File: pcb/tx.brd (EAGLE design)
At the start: 28 x 35 mm, 52 parts, among them U3 MCP73831T-2ACI/OT, Y1 CRYSTAL-26MHZSMD-3.2X2.5

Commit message: txrx rev2 finished
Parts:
- added R13: 22K, joyAnalog:0805
- moved SJ2 3.86 mm to (23.9, 5.59), turned to 90 degrees
- moved LED2 0.55 mm to (5.84, 23.3)
- moved U$5 0.50 mm to (2.50, 27.0)
- moved U$6 0.50 mm to (25.5, 27.0)
- moved U$10 0.23 mm to (1.68, 21.6)
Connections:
- new net N$36: SJ2.2, U$2.6
- net +3V3: now also U$10.P$1, U$10.P$4
- net GND: now also R13.2; no longer U$10.P$1, U$10.P$4
- net N$30: now also R13.1
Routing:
- net GND: track 39.6 -> 30.6 mm
- net N$36: track 0.00 -> 7.97 mm, vias 0 -> 1
- net +3V3: track 43.8 -> 48.0 mm, vias 7 -> 9
- net N$30: track 26.7 -> 28.8 mm
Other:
- board text added: "ADDR"
- board text added: "REV2 FEB19"
- board text added: "dekuNukem 2018"
- board text removed: "TEST"
- board text removed: "dayTripper TX dekuNukem 2018"

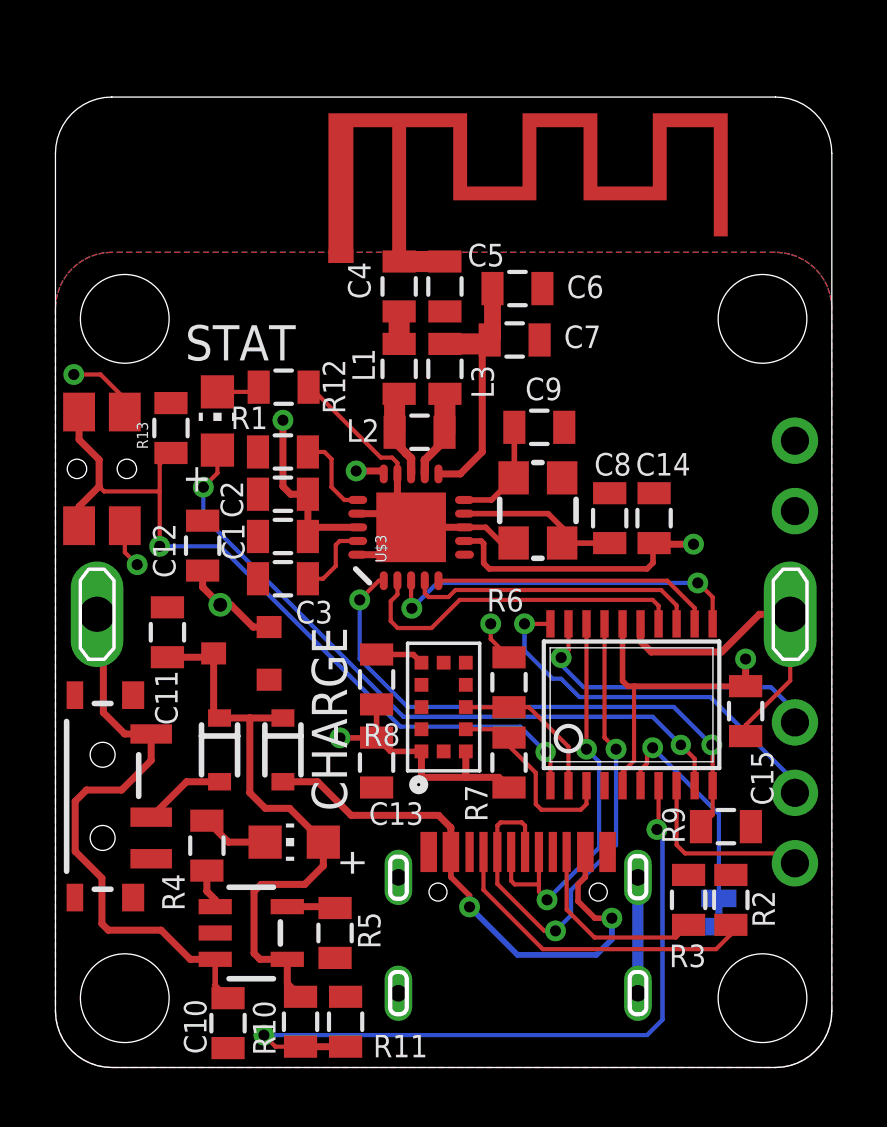
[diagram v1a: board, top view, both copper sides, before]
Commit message: switched to chip antenna
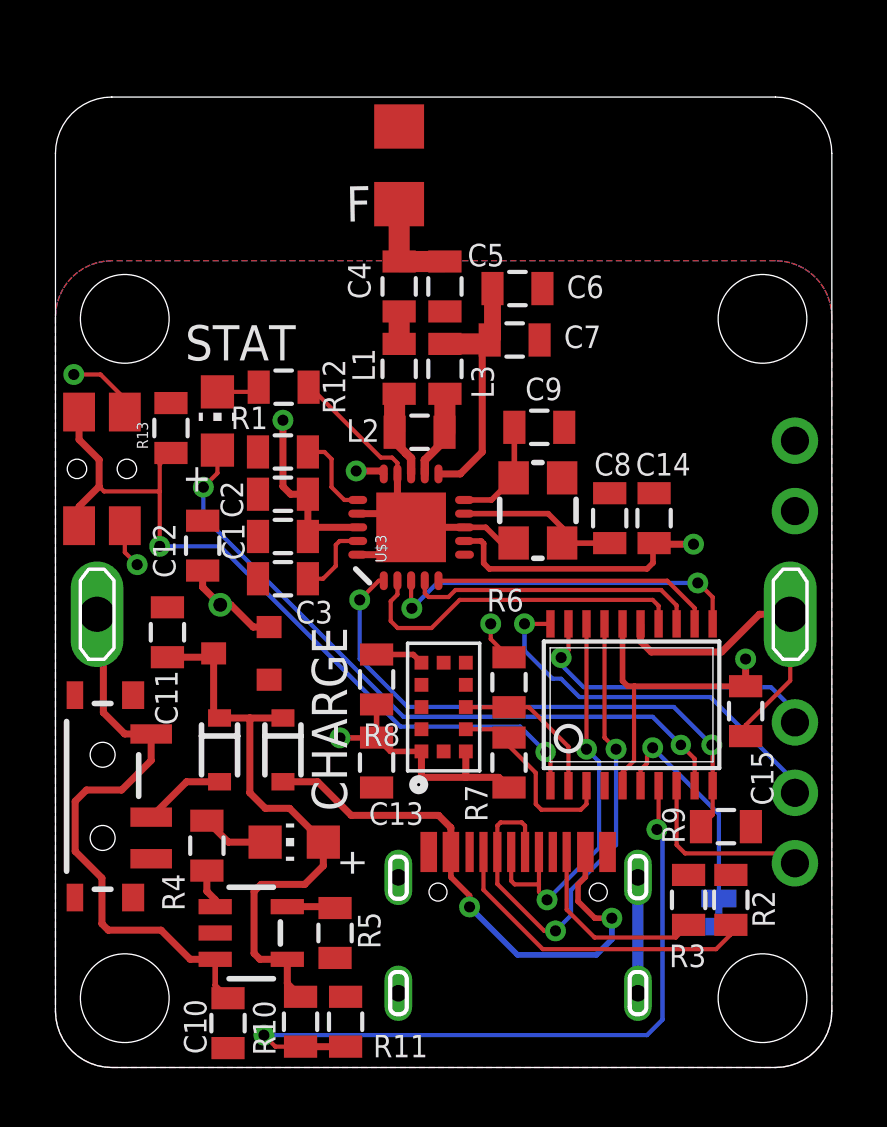
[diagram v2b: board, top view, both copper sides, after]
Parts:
- removed E1: ANT, SparkFun-RF:TRACE_ANTENNA_2.4GHZ_15.2MM
- added U$1: 1206ANT_DEV, 3pos_slide_switch:C1206
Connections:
- net GND: no longer E1.GND
- net N$5: now also U$1.1; no longer E1.ANT
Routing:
- net N$5: track 1.85 -> 3.72 mm
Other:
- board text added: "DFU"
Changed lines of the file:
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@@
 <grid distance="2" unitdist="mil" unit="mil" style="lines" multiple="1" display="no" altdistance="5" altunitdist="mil" altunit="mil"/>
 <layers>
-<layer number="1" name="Top" color="4" fill="1" visible="no" active="yes"/>
+<layer number="1" name="Top" color="4" fill="1" visible="yes" active="yes"/>
 <layer number="2" name="Route2" color="16" fill="1" visible="no" active="no"/>
 <layer number="3" name="Route3" color="17" fill="1" visible="no" active="no"/>
@@
 <layer number="19" name="Unrouted" color="6" fill="1" visible="yes" active="yes"/>
 <layer number="20" name="Dimension" color="24" fill="1" visible="yes" active="yes"/>
-<layer number="21" name="tPlace" color="7" fill="1" visible="no" active="yes"/>
+<layer number="21" name="tPlace" color="7" fill="1" visible="yes" active="yes"/>
 <layer number="22" name="bPlace" color="7" fill="1" visible="yes" active="yes"/>
-<layer number="23" name="tOrigins" color="15" fill="1" visible="no" active="yes"/>
+<layer number="23" name="tOrigins" color="15" fill="1" visible="yes" active="yes"/>
 <layer number="24" name="bOrigins" color="15" fill="1" visible="yes" active="yes"/>
-<layer number="25" name="tNames" color="7" fill="1" visible="no" active="yes"/>
+<layer number="25" name="tNames" color="7" fill="1" visible="yes" active="yes"/>
 <layer number="26" name="bNames" color="7" fill="1" visible="yes" active="yes"/>
 <layer number="27" name="tValues" color="7" fill="1" visible="no" active="yes"/>
@@
 <layer number="37" name="tTest" color="7" fill="1" visible="no" active="yes"/>
 <layer number="38" name="bTest" color="7" fill="1" visible="no" active="yes"/>
-<layer number="39" name="tKeepout" color="4" fill="11" visible="no" active="yes"/>
+<layer number="39" name="tKeepout" color="4" fill="11" visible="yes" active="yes"/>
 <layer number="40" name="bKeepout" color="1" fill="11" visible="yes" active="yes"/>
-<layer number="41" name="tRestrict" color="4" fill="10" visible="no" active="yes"/>
+<layer number="41" name="tRestrict" color="4" fill="10" visible="yes" active="yes"/>
 <layer number="42" name="bRestrict" color="1" fill="10" visible="yes" active="yes"/>
 <layer number="43" name="vRestrict" color="2" fill="10" visible="no" active="yes"/>
@@
 <layer number="49" name="Reference" color="7" fill="1" visible="no" active="yes"/>
 <layer number="50" name="dxf" color="7" fill="1" visible="no" active="no"/>
-<layer number="51" name="tDocu" color="7" fill="1" visible="no" active="yes"/>
+<layer number="51" name="tDocu" color="7" fill="1" visible="yes" active="yes"/>
 <layer number="52" name="bDocu" color="7" fill="1" visible="yes" active="yes"/>
 <layer number="53" name="tGND_GNDA" color="7" fill="1" visible="no" active="no"/>
@@
 <wire x1="2.032" y1="0" x2="25.968" y2="0" width="0" layer="20"/>
 <wire x1="25.968" y1="0" x2="28" y2="2.032" width="0" layer="20" curve="90"/>
-<polygon width="0.254" layer="41">
-<vertex x="11.8364" y="28.7782"/>
-<vertex x="11.8364" y="29.8958"/>
-<vertex x="12.8524" y="29.8958"/>
-<vertex x="12.8524" y="28.7782"/>
-</polygon>
 <text x="25.273" y="21.971" size="1.27" layer="26" rot="MR0">GND</text>
 <text x="25.273" y="19.431" size="1.27" layer="26" rot="MR0">3V</text>
@@
 <text x="8.6614" y="26.7716" size="1.27" layer="25" rot="R180">STAT</text>
 <text x="23.0886" y="6.3754" size="0.8128" layer="26" rot="MR270">ADDR</text>
+<text x="1.9304" y="22.7584" size="1.27" layer="26" rot="MR270">DFU</text>
 </plain>
 <attributes>
@@
 </element>
 <element name="SJ2" library="SparkFun-Jumpers" package="SMT-JUMPER_2_NC_TRACE_NO-SILK" value="JUMPER-SMT_2_NC_TRACE_NO-SILK" x="23.9268" y="5.588" smashed="yes" rot="MR90"/>
-<element name="E1" library="SparkFun-RF" package="TRACE_ANTENNA_2.4GHZ_15.2MM" value="ANT" x="12.3952" y="29.5148" smashed="yes">
-<attribute name="VALUE" x="12.3952" y="30.5308" size="0.6096" layer="27" font="vector" ratio="20" align="top-center"/>
-</element>
 <element name="U$4" library="my_usbc_16p" package="USBC_16P_FOOT" value="USBC_16P" x="13.462" y="7.7724"/>
 <element name="R13" library="joyAnalog" package="0805" value="22K" x="4.1656" y="23.0632" rot="R90"/>
+<element name="U$1" library="3pos_slide_switch" package="C1206" value="1206ANT_DEV" x="12.3952" y="32.5374" rot="R90"/>
 </elements>
 <signals>
@@
 <contactref element="BT1" pad="2"/>
 <polygon width="0.1524" layer="1" isolate="0.254">
-<vertex x="28" y="2.032"/>
-<vertex x="28" y="27.3696" curve="90"/>
-<vertex x="25.968" y="29.4016"/>
-<vertex x="2.032" y="29.4016" curve="90"/>
-<vertex x="0" y="27.3696"/>
+<vertex x="25.968" y="29.0968"/>
+<vertex x="2.032" y="29.0968" curve="90"/>
+<vertex x="0" y="27.0648"/>
 <vertex x="0" y="2.032" curve="90"/>
 <vertex x="2.032" y="0"/>
 <vertex x="25.968" y="0" curve="90"/>
+<vertex x="28" y="2.032"/>
+<vertex x="28" y="27.0648" curve="90"/>
 </polygon>
 <contactref element="C10" pad="2"/>
@@
 <wire x1="11.7348" y1="21.9964" x2="9.1948" y2="24.5364" width="0.1524" layer="1"/>
 <wire x1="9.1948" y1="24.5364" x2="9.1296" y2="24.5364" width="0.1524" layer="1"/>
-<contactref element="E1" pad="GND"/>
 <contactref element="U$4" pad="B11A12"/>
 <contactref element="U$4" pad="P$13"/>
@@
 <contactref element="C12" pad="1"/>
 <polygon width="0.1524" layer="16" isolate="0.254">
-<vertex x="28" y="2.032"/>
-<vertex x="28" y="27.3696" curve="90"/>
-<vertex x="25.968" y="29.4016"/>
-<vertex x="2.032" y="29.4016" curve="90"/>
-<vertex x="0" y="27.3696"/>
+<vertex x="25.968" y="29.0968"/>
+<vertex x="2.032" y="29.0968" curve="90"/>
+<vertex x="0" y="27.0648"/>
 <vertex x="0" y="2.032" curve="90"/>
 <vertex x="2.032" y="0"/>
 <vertex x="25.968" y="0" curve="90"/>
+<vertex x="28" y="2.032"/>
+<vertex x="28" y="27.0648" curve="90"/>
 </polygon>
 <via x="5.9436" y="16.6878" extent="1-16" drill="0.5"/>
@@
 <contactref element="C4" pad="2"/>
 <contactref element="C5" pad="1"/>
-<contactref element="E1" pad="ANT"/>
 <wire x1="14.0462" y1="29.0686" x2="12.3952" y2="29.0686" width="0.762" layer="1"/>
-<wire x1="12.3952" y1="29.0686" x2="12.3952" y2="29.2648" width="0.508" layer="1"/>
+<contactref element="U$1" pad="1"/>
+<wire x1="12.3952" y1="29.0686" x2="12.3952" y2="31.1374" width="0.762" layer="1"/>
 </signal>
 <signal name="N$6">

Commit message: GND plane, trace antenna, clean up
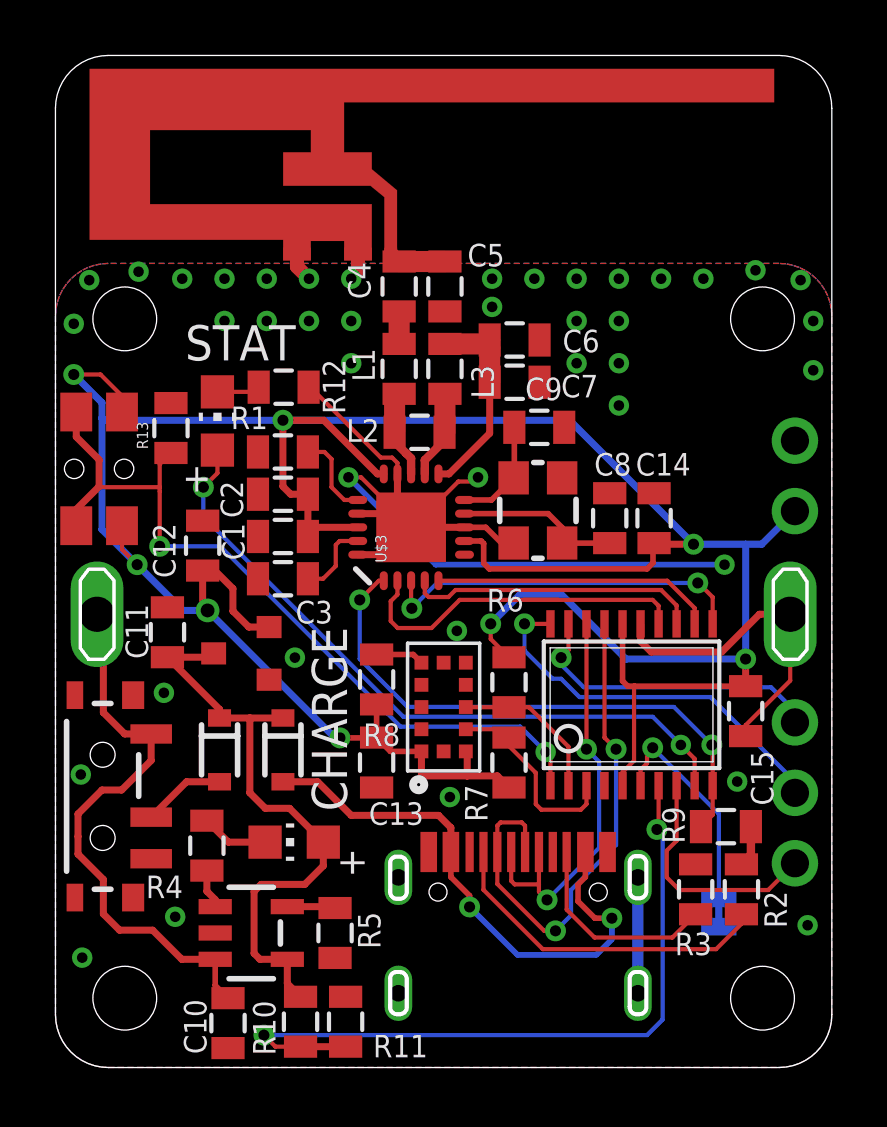
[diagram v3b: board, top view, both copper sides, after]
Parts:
- removed U$5, U$6, U$7, U$8: M3_MOUNTING_HOLE, L1:M3_MOUNTING_HOLE_PACK
- added E1: ANTENNA, esp32-thing-temp:TRACE_ANTENNA_2.4GHZ_25.7MM_TUNED
- added U$12, U$13, U$14: M2_SCREW_DEV, 3pos_slide_switch:M2_SCREW_FOOT
- U$1: value 1206ANT_DEV -> M2_SCREW_DEV; device 3pos_slide_switch:C1206 -> 3pos_slide_switch:M2_SCREW_FOOT
- moved U$1 31.6 mm to (2.50, 2.50), turned to 0 degrees
- moved C6 1.86 mm to (16.6, 26.2)
- moved C7 1.52 mm to (16.6, 24.7)
- moved R2 0.54 mm to (24.7, 6.43)
- moved R3 0.46 mm to (23.1, 6.43)
- moved U$10 0.10 mm to (1.57, 21.6)
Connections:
- net +3V3: no longer SJ2.1
- net GND: now also E1.GND, E1.GND2, SJ2.1
- net N$5: now also E1.ANT; no longer U$1.1
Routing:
- net +3V3: track 48.0 -> 112.8 mm, vias 9 -> 8
- net GND: track 30.6 -> 54.3 mm, vias 0 -> 41
- net N$8: track 9.63 -> 7.41 mm
- net N$33: track 6.68 -> 8.66 mm
- net N$5: track 3.72 -> 2.07 mm
- net N$27: track 21.3 -> 22.1 mm
- net N$25: track 21.0 -> 20.4 mm
- net N$11: track 11.7 -> 12.3 mm
- added copper zone on layer 16, net GND
- removed copper zone on layer 16, net +3V3
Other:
- board size 28 x 35 mm -> 28 x 36.5 mm
- board text added: "CH"
- board text added: "REV3 FEB19"
- board text removed: "ADDR"
- board text removed: "REV2 FEB19"

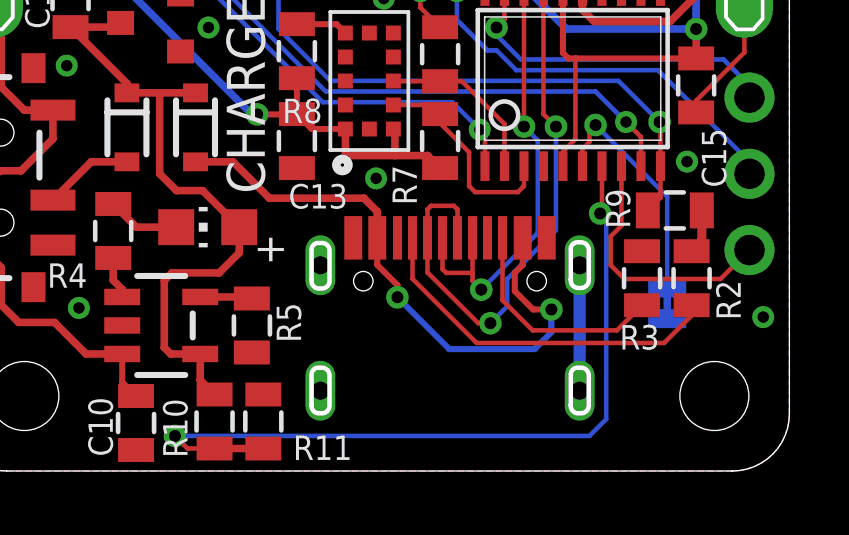
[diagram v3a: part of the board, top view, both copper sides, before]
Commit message: changed copyright date
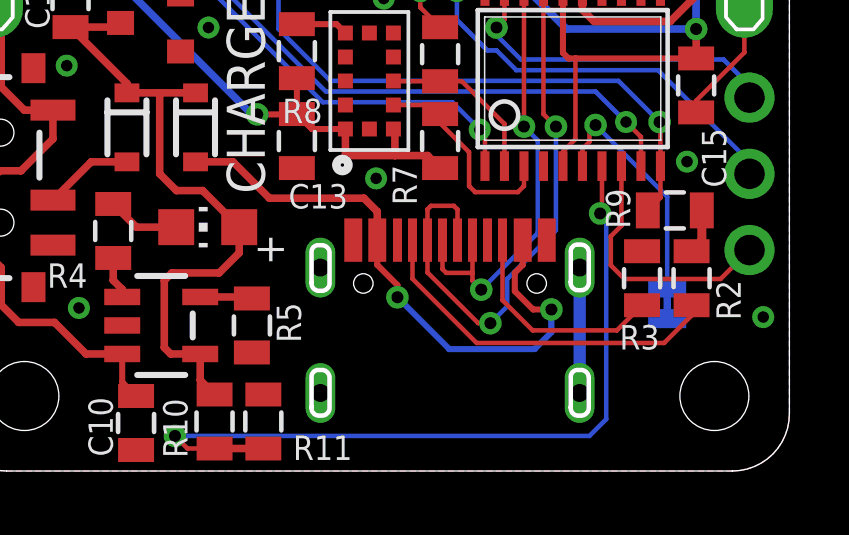
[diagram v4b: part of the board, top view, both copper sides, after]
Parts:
- moved U$4 0.08 mm to (13.5, 7.70)
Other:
- board text added: "dekuNukem 2019"
- board text removed: "dekuNukem 2018"
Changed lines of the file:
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@@
 <setting verticaltext="up"/>
 </settings>
-<grid distance="2" unitdist="mil" unit="mil" style="lines" multiple="1" display="no" altdistance="1" altunitdist="mil" altunit="mil"/>
+<grid distance="1" unitdist="mil" unit="mil" style="lines" multiple="1" display="no" altdistance="1" altunitdist="mil" altunit="mil"/>
 <layers>
 <layer number="1" name="Top" color="4" fill="1" visible="yes" active="yes"/>
@@
 <text x="25.273" y="9.271" size="1.27" layer="26" rot="MR0">CLK</text>
 <text x="25.273" y="6.731" size="1.27" layer="26" rot="MR0">TX</text>
-<text x="14" y="31.017" size="1.016" layer="26" font="vector" rot="MR0" align="center">dekuNukem 2018</text>
+<text x="14" y="31.017" size="1.016" layer="26" font="vector" rot="MR0" align="center">dekuNukem 2019</text>
 <text x="14" y="33.205" size="1.27" layer="26" rot="MR0" align="center">git.io/daytripper</text>
 <text x="16.8402" y="2.032" size="1.27" layer="26" rot="MR0" align="center">REV3
@@
 </element>
 <element name="SJ2" library="SparkFun-Jumpers" package="SMT-JUMPER_2_NC_TRACE_NO-SILK" value="JUMPER-SMT_2_NC_TRACE_NO-SILK" x="23.9268" y="5.588" smashed="yes" rot="MR90"/>
-<element name="U$4" library="my_usbc_16p" package="USBC_16P_FOOT" value="USBC_16P" x="13.462" y="7.7724"/>
+<element name="U$4" library="my_usbc_16p" package="USBC_16P_FOOT" value="USBC_16P" x="13.462" y="7.6962"/>
 <element name="R13" library="joyAnalog" package="0805" value="22K" x="4.1656" y="23.0632" rot="R90"/>
 <element name="E1" library="esp32-thing-temp" package="TRACE_ANTENNA_2.4GHZ_25.7MM_TUNED" value="ANTENNA" x="12.0904" y="29.1084"/>
@@
 <wire x1="25.3884" y1="16.346" x2="26.5" y2="16.346" width="0.254" layer="1"/>
 <wire x1="24.0284" y1="14.986" x2="25.3884" y2="16.346" width="0.254" layer="1"/>
-<wire x1="21.007" y1="6.8574" x2="21.007" y2="2.6774" width="0.4064" layer="16"/>
+<wire x1="21.007" y1="6.7812" x2="21.007" y2="2.6012" width="0.4064" layer="16"/>
 <wire x1="26.5" y1="16.346" x2="26.5" y2="13.9524" width="0.1524" layer="1"/>
 <wire x1="24.892" y1="12.3444" x2="24.892" y2="11.9524" width="0.1524" layer="1"/>
@@
 <contactref element="U$4" pad="B5"/>
 <wire x1="22.2504" y1="4.688" x2="19.442" y2="4.688" width="0.1524" layer="1"/>
-<wire x1="18.437" y1="5.693" x2="18.437" y2="7.7724" width="0.1524" layer="1"/>
+<wire x1="18.437" y1="5.693" x2="18.437" y2="7.6962" width="0.1524" layer="1"/>
 <wire x1="19.442" y1="4.688" x2="18.437" y2="5.693" width="0.1524" layer="1"/>
 <wire x1="23.0886" y1="5.5262" x2="22.2504" y2="4.688" width="0.1524" layer="1"/>
@@
 <wire x1="24.7396" y1="5.1816" x2="23.8252" y2="4.2672" width="0.1524" layer="1"/>
 <wire x1="23.8252" y1="4.2672" x2="17.5768" y2="4.2672" width="0.1524" layer="1"/>
-<wire x1="15.437" y1="6.407" x2="15.437" y2="7.7724" width="0.1524" layer="1"/>
+<wire x1="15.437" y1="6.407" x2="15.437" y2="7.6962" width="0.1524" layer="1"/>
 <wire x1="17.5768" y1="4.2672" x2="15.437" y2="6.407" width="0.1524" layer="1"/>
 </signal>
@@
 <contactref element="U$4" pad="B4A9"/>
 <wire x1="10.668" y1="9.0932" x2="13.8176" y2="9.0932" width="0.254" layer="1"/>
-<wire x1="14.262" y1="8.6488" x2="14.262" y2="7.7724" width="0.254" layer="1"/>
+<wire x1="14.262" y1="8.6488" x2="14.262" y2="7.6962" width="0.254" layer="1"/>
 <wire x1="13.8176" y1="9.0932" x2="14.262" y2="8.6488" width="0.254" layer="1"/>
-<wire x1="19.112" y1="7.7724" x2="19.112" y2="6.8692" width="0.2032" layer="1"/>
+<wire x1="19.112" y1="7.6962" x2="19.112" y2="6.8692" width="0.2032" layer="1"/>
 <wire x1="19.112" y1="6.8692" x2="18.8468" y2="6.604" width="0.2032" layer="1"/>
 <wire x1="18.8468" y1="6.604" x2="18.8468" y2="5.9944" width="0.2032" layer="1"/>
@@
 <via x="14.9352" y="5.7912" extent="1-16" drill="0.4"/>
 <wire x1="14.9352" y1="5.7912" x2="14.9352" y2="6.1976" width="0.2032" layer="1"/>
-<wire x1="14.262" y1="6.8708" x2="14.262" y2="7.7724" width="0.2032" layer="1"/>
+<wire x1="14.262" y1="6.8708" x2="14.262" y2="7.6962" width="0.2032" layer="1"/>
 <wire x1="14.9352" y1="6.1976" x2="14.262" y2="6.8708" width="0.2032" layer="1"/>
 </signal>
@@
 <via x="19.1516" y="11.4808" extent="1-16" drill="0.4"/>
 <via x="17.7292" y="6.0452" extent="1-16" drill="0.4"/>
-<wire x1="17.437" y1="7.7724" x2="17.437" y2="6.604" width="0.1524" layer="1"/>
+<wire x1="17.437" y1="7.6962" x2="17.437" y2="6.604" width="0.1524" layer="1"/>
 <wire x1="17.437" y1="6.604" x2="17.437" y2="6.3374" width="0.1524" layer="1"/>
 <wire x1="17.437" y1="6.3374" x2="17.7292" y2="6.0452" width="0.1524" layer="1"/>
-<wire x1="16.437" y1="7.7724" x2="16.437" y2="6.7278" width="0.1524" layer="1"/>
+<wire x1="16.437" y1="7.6962" x2="16.437" y2="6.7278" width="0.1524" layer="1"/>
 <wire x1="16.437" y1="6.7278" x2="16.5608" y2="6.604" width="0.1524" layer="1"/>
 <wire x1="16.5608" y1="6.604" x2="17.437" y2="6.604" width="0.1524" layer="1"/>
@@
 <contactref element="U$4" pad="B7"/>
 <contactref element="U$2" pad="17"/>
-<wire x1="16.937" y1="7.7724" x2="16.937" y2="8.717" width="0.1524" layer="1"/>
+<wire x1="16.937" y1="7.6962" x2="16.937" y2="8.717" width="0.1524" layer="1"/>
 <wire x1="16.937" y1="8.717" x2="16.8148" y2="8.8392" width="0.1524" layer="1"/>
 <wire x1="16.8148" y1="8.8392" x2="16.0528" y2="8.8392" width="0.1524" layer="1"/>
-<wire x1="15.937" y1="8.7234" x2="15.937" y2="7.7724" width="0.1524" layer="1"/>
+<wire x1="15.937" y1="8.7234" x2="15.937" y2="7.6962" width="0.1524" layer="1"/>
 <wire x1="16.0528" y1="8.8392" x2="15.937" y2="8.7234" width="0.1524" layer="1"/>
 <wire x1="19.8022" y1="15.9988" x2="19.8022" y2="11.897" width="0.1524" layer="1"/>
@@
 <via x="18.034" y="4.9276" extent="1-16" drill="0.4"/>
 <wire x1="18.034" y1="4.9276" x2="17.6276" y2="4.9276" width="0.1524" layer="1"/>
-<wire x1="15.937" y1="6.6182" x2="15.937" y2="7.7724" width="0.1524" layer="1"/>
+<wire x1="15.937" y1="6.6182" x2="15.937" y2="7.6962" width="0.1524" layer="1"/>
 <wire x1="17.6276" y1="4.9276" x2="15.937" y2="6.6182" width="0.1524" layer="1"/>
 <wire x1="20.2184" y1="11.4808" x2="20.2184" y2="8.0264" width="0.1524" layer="16"/>
